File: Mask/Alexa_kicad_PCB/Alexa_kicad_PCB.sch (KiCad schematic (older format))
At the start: 48 parts, among them J1 Jack-DC, J2 USB_B_Micro, J3 Conn_01x07_Male, M1 Motor_Servo, M2 Motor_Servo, M3 Motor_Servo, U1 TLV2372, U2 LM1117-3.3, U3 STM32F405RGTx, X1 1503_09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

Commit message: v0.2 routing started
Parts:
- C1, C2, C3, C4, C5, C6: footprint Capacitor_SMD:C_0805_2012Metric -> Capacitor_SMD:C_0603_1608Metric
- C7, C8: renamed from C?; footprint (none) -> Capacitor_SMD:C_0603_1608Metric
- D3, D4, D5, D6, D7: renamed from D?; footprint (none) -> LED_SMD:LED_0603_1608Metric
- R1, R10, R2, R4, R9: footprint Resistor_SMD:R_0805_2012Metric -> Resistor_SMD:R_0603_1608Metric
- R11, R12, R13, R14, R15, R16, R17, R18, R3, R5, R6, R7, R8: renamed from R?; footprint (none) -> Resistor_SMD:R_0603_1608Metric
- SW1, SW2, SW3: renamed from SW?; footprint (none) -> Button_Switch_SMD:SW_SPST_B3U-1000P

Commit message: v0.2 routing completed
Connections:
- net PB3-USR_SW: now also SW3.2
- net USR_SW: no longer SW3.2
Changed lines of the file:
@@
 BOOT0-(DFU)
 Text Label 10600 4325 0    50   ~ 0
-USR_SW
+PB3-USR_SW
 $Comp
 L Switch:SW_Push SW3

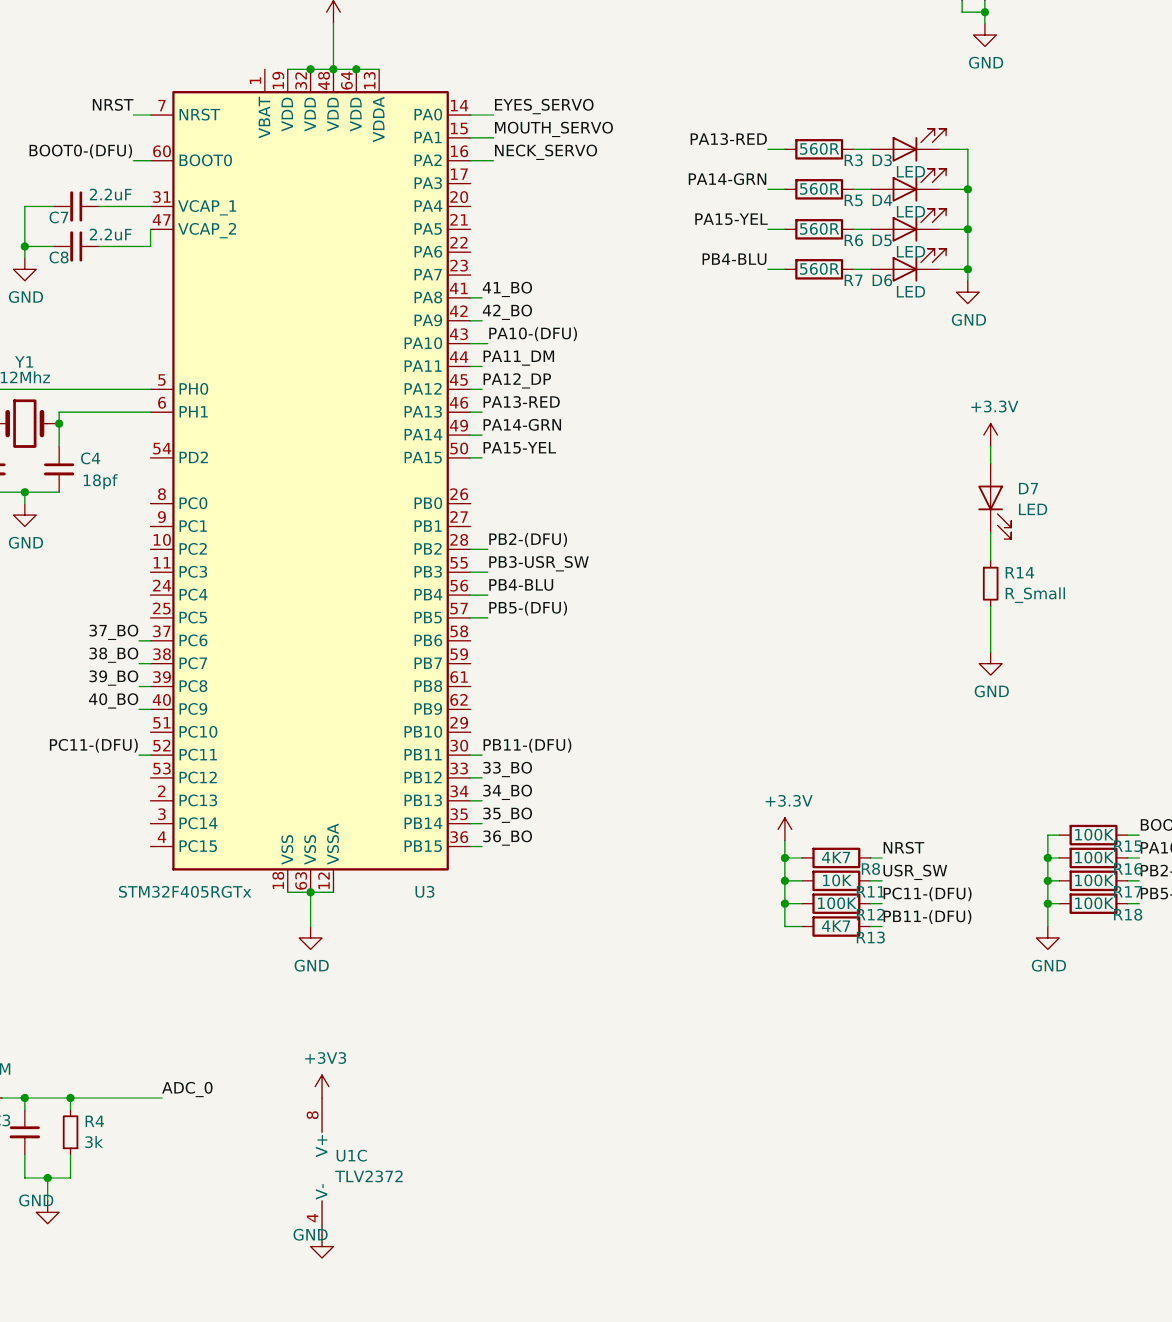
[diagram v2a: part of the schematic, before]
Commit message: fixed missing envelope out trace
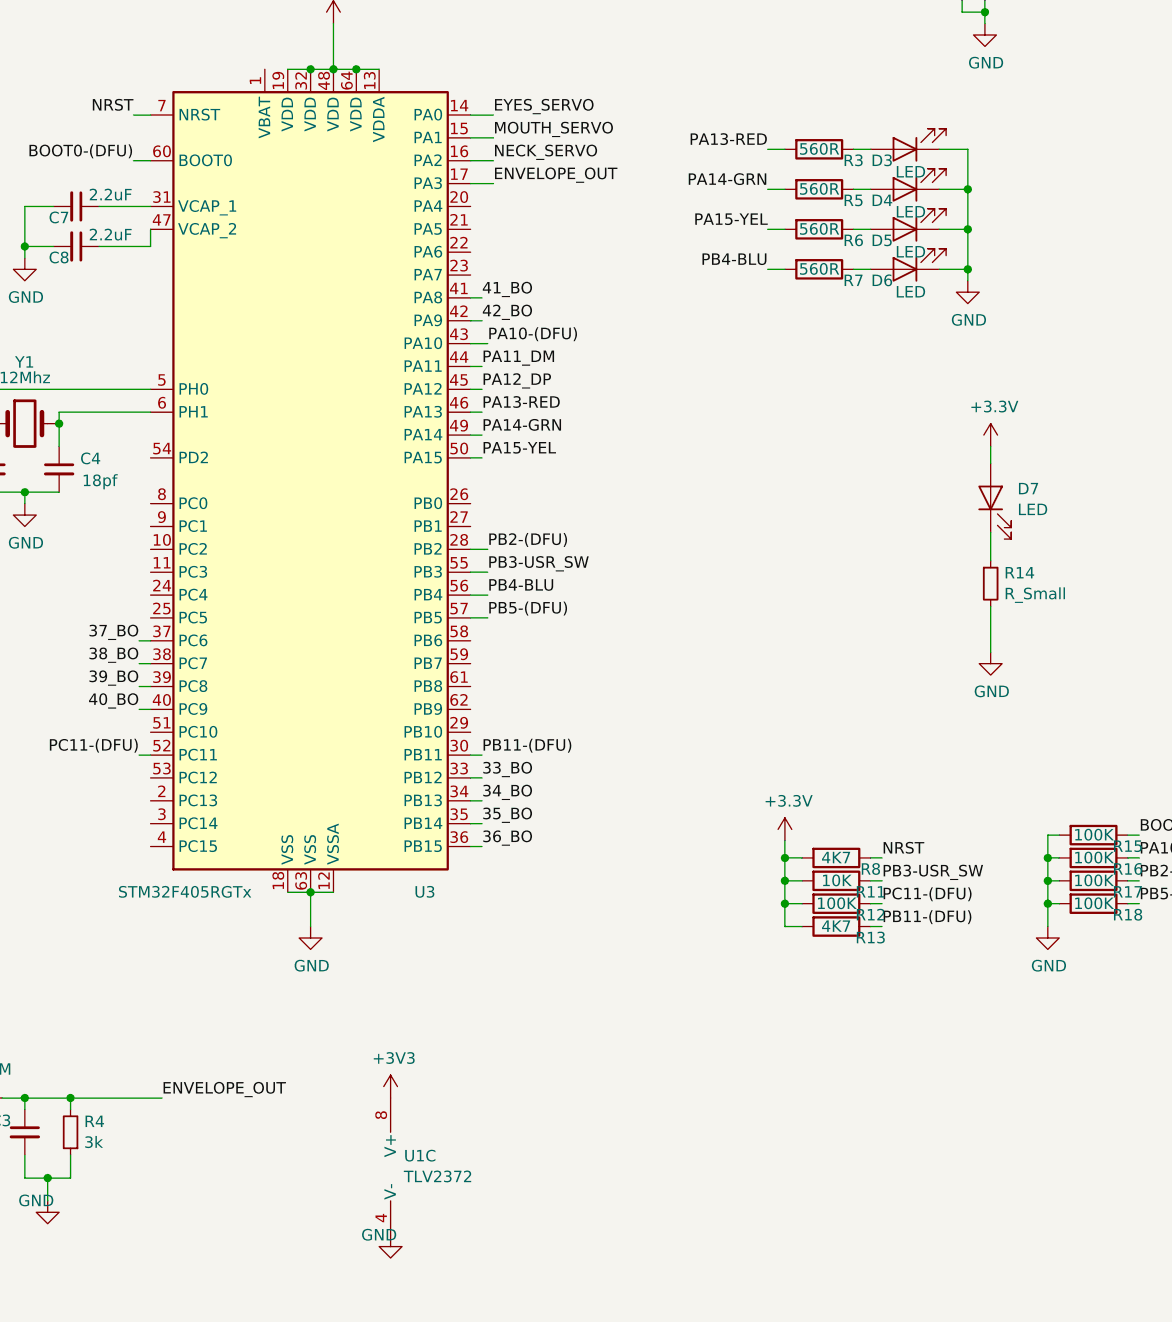
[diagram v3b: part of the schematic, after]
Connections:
- net ADC_0 is gone; now on net ENVELOPE_OUT: C3.1, D1.3 (K), R4.2
- net USR_SW is gone; now on net PB3-USR_SW: R11.1
- net ENVELOPE_OUT: now reaches U3.17 (PA3)
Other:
- moved on the sheet: U1C
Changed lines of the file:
@@
 L power:GND #PWR0114
 U 1 1 5F10A0DF
-P 4700 7150
-F 0 "#PWR0114" H 4700 6900 50  0001 C CNN
-F 1 "GND" H 4650 7150 50  0000 C CNN
-F 2 "" H 4700 7150 50  0001 C CNN
-F 3 "" H 4700 7150 50  0001 C CNN
-	1    4700 7150
+P 5000 7150
+F 0 "#PWR0114" H 5000 6900 50  0001 C CNN
+F 1 "GND" H 4950 7150 50  0000 C CNN
+F 2 "" H 5000 7150 50  0001 C CNN
+F 3 "" H 5000 7150 50  0001 C CNN
+	1    5000 7150
 	1    0    0    -1
 $EndComp
@@
 L power:+3V3 #PWR0116
 U 1 1 5F111596
-P 4700 6550
-F 0 "#PWR0116" H 4700 6400 50  0001 C CNN
-F 1 "+3V3" H 4715 6723 50  0000 C CNN
-F 2 "" H 4700 6550 50  0001 C CNN
-F 3 "" H 4700 6550 50  0001 C CNN
-	1    4700 6550
+P 5000 6550
+F 0 "#PWR0116" H 5000 6400 50  0001 C CNN
+F 1 "+3V3" H 5015 6723 50  0000 C CNN
+F 2 "" H 5000 6550 50  0001 C CNN
+F 3 "" H 5000 6550 50  0001 C CNN
+	1    5000 6550
 	1    0    0    -1
 $EndComp
@@
 Connection ~ 3600 6550
 Text Label 4000 6550 0    50   ~ 0
-ADC_0
+ENVELOPE_OUT
 $Comp
 L power:+5V #PWR0118
@@
 L Amplifier_Operational:TLV2372 U1
 U 3 1 5F22E681
-P 4800 6850
-F 0 "U1" H 4758 6896 50  0000 L CNN
-F 1 "TLV2372" H 4758 6805 50  0000 L CNN
-F 2 "Package_SO:SOIC-8_3.9x4.9mm_P1.27mm" H 4800 6850 50  0001 C CNN
-F 3 "http://www.ti.com/lit/ds/symlink/tlv2375.pdf" H 4800 6850 50  0001 C CNN
-	3    4800 6850
+P 5100 6850
+F 0 "U1" H 5058 6896 50  0000 L CNN
+F 1 "TLV2372" H 5058 6805 50  0000 L CNN
+F 2 "Package_SO:SOIC-8_3.9x4.9mm_P1.27mm" H 5100 6850 50  0001 C CNN
+F 3 "http://www.ti.com/lit/ds/symlink/tlv2375.pdf" H 5100 6850 50  0001 C CNN
+	3    5100 6850
 	1    0    0    -1
 $EndComp
@@
 $EndComp
 Text Label 7150 5600 0    50   ~ 0
-USR_SW
+PB3-USR_SW
 Text Label 7150 5500 0    50   ~ 0
 NRST
@@
 Wire Wire Line
 	5350 4250 5425 4250
+Text Label 5450 2550 0    50   ~ 0
+ENVELOPE_OUT
+Wire Wire Line
+	5350 2550 5450 2550
 $EndSCHEMATC

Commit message: changed c3 to 1206, generated jlcpcb fab files
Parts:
- C3: footprint Capacitor_SMD:C_0603_1608Metric -> Capacitor_SMD:C_1206_3216Metric
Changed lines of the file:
@@
 F 0 "C3" H 3250 6750 50  0000 L CNN
 F 1 "47uF" H 3050 6650 50  0000 L CNN
-F 2 "Capacitor_SMD:C_0603_1608Metric" H 3400 6700 50  0001 C CNN
+F 2 "Capacitor_SMD:C_1206_3216Metric" H 3400 6700 50  0001 C CNN
 F 3 "~" H 3400 6700 50  0001 C CNN
 	1    3400 6700
